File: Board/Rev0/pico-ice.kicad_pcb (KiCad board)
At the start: 2 copper layers, 52 x 51 mm, 121 parts, among them J1 Connector_USB_B_Micro, J1 USB_B_Micro, J2 6X2 Female Header, J2 Conn_01x02, J3 6X2 Female Header, J3 Conn_02x18_Odd_Even, J4 6X2 Female Header, J4 Conn_02x18_Odd_Even, J5 Conn_ARM_JTAG_SWD_10, J6 6X2 Female Header, J7 6X2 Female Header, J8 6X2 Female Header, J9 BOOT_SEL, SW1 PTS820 J25K SMTR LFS, SW2 PTS820 J25K SMTR LFS, U1 NCP1117ST33T3G, U2 W25Q128JVS, U2 W25Q32JVSSIQ, U3 RP2040, U4 CL9293A12L5M, U5 APS6404L-3SQN-SN, U6 ICE40UP5K-SG48ITR, U8 W25Q32JVSSIQ, Y1 ABLS-12.000MHZ-B4-T

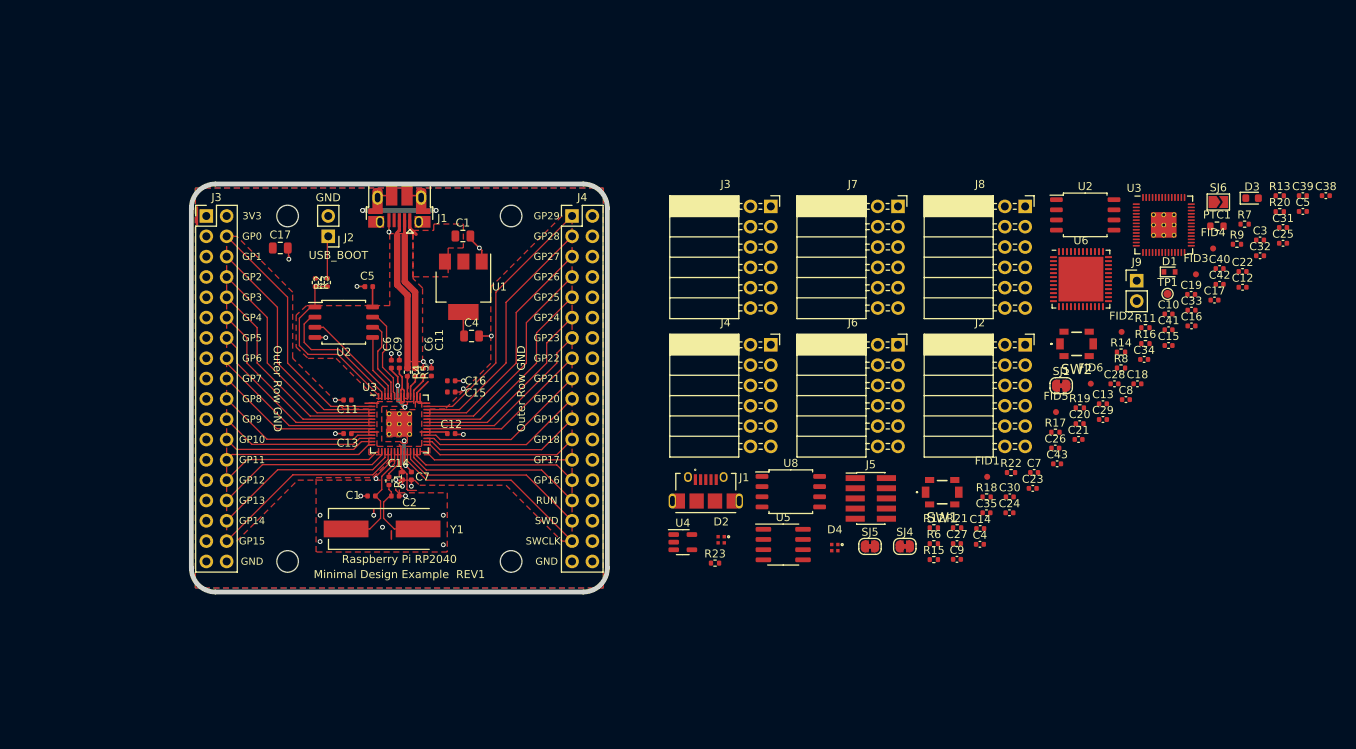
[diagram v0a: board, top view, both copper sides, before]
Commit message: Rough placement, needs work to compress this and center everything into 0.1" centers
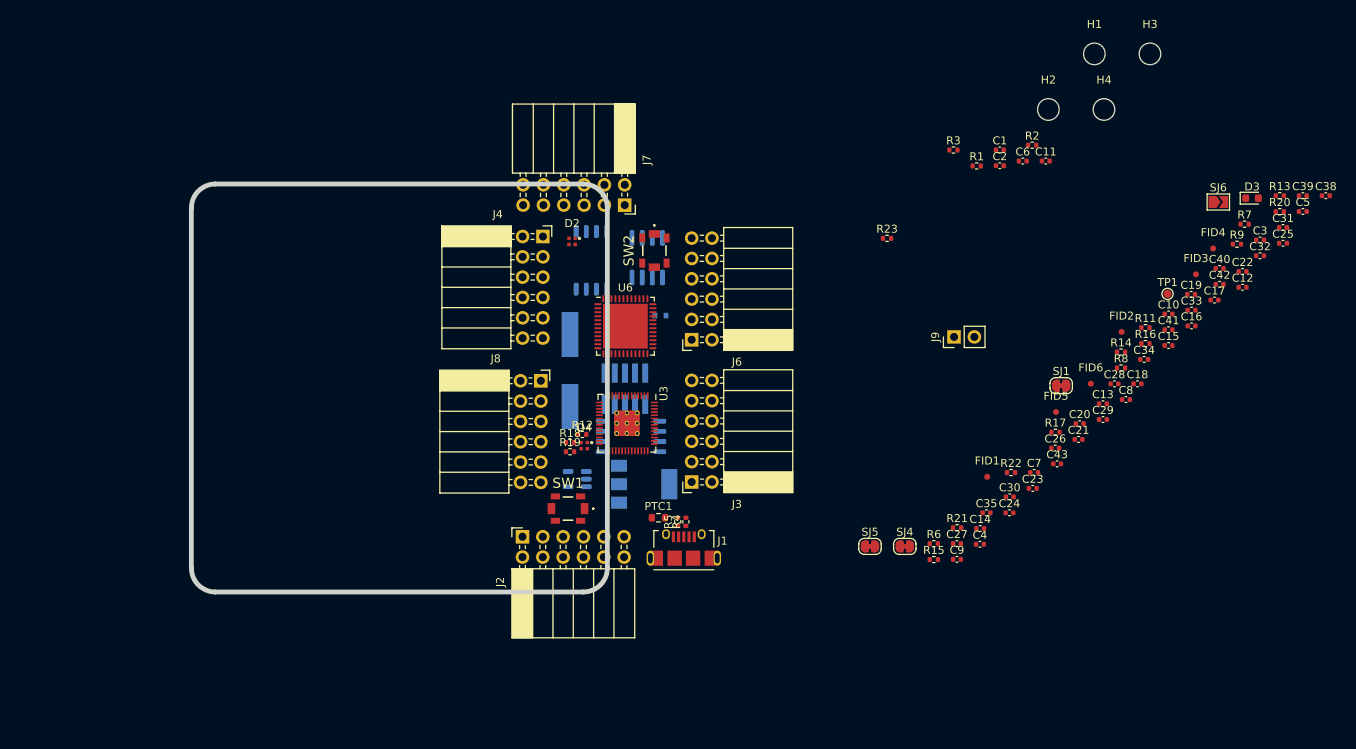
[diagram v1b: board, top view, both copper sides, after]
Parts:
- removed the C1 at (107.9, 76.5)
- removed the C1 at (96.5, 109.0)
- removed the C11 at (104.0, 93.5)
- removed the C11 at (93.5, 97.0)
- removed the C12 at (106.5, 101.2)
- removed the C13 at (93.5, 101.2)
- removed the C14 at (100.4, 106.5)
- removed the C15 at (106.5, 96.0)
- removed the C16 at (106.5, 94.6)
- removed the C17 at (85.1, 78.0)
- removed the C4 at (109.0, 89.0)
- removed the C5 at (96.2, 82.8)
- removed the C6 at (103.0, 93.5)
- removed the C6 at (99.0, 92.5)
- removed the C7 at (101.5, 106.5)
- removed the C9 at (100.0, 92.5)
- removed the J1 at (100.0, 71.7)
- removed the J2 at (91.1, 76.5)
- removed the J3 at (75.9, 74.0)
- removed the J4 at (121.6, 74.0)
- removed the U2 at (93.0, 87.3)
- removed the U3 at (100.0, 100.0)
- added C1: 27p, Capacitor_SMD:C_0402_1005Metric, F.Cu at (175.1, 65.7)
- added C11: 1u, Capacitor_SMD:C_0402_1005Metric, F.Cu at (180.8, 67.1)
- added C6: 1u, Capacitor_SMD:C_0402_1005Metric, F.Cu at (177.9, 67.1)
- D1, J5, U1, U2, U4, U5, U8, Y1: moved to B.Cu
- moved H4 116.6 mm to (188.1, 60.7)
- moved H1 102.9 mm to (186.9, 53.7)
- moved H3 102.0 mm to (193.8, 53.7)
- moved R2 89.8 mm to (179.1, 65.2), turned to 0 degrees
- moved C2 86.1 mm to (175.1, 67.7)
- moved R1 83.4 mm to (172.2, 67.7), turned to 0 degrees
- moved R3 81.5 mm to (169.3, 65.8), turned to 0 degrees
- moved PTC1 78.8 mm to (132.4, 111.7)
- moved U3 71.5 mm to (128.4, 99.9), turned to -90 degrees
- moved H2 68.5 mm to (181.1, 60.7)
- moved J2 67.3 mm to (115.4, 114.1), turned to 90 degrees
- moved J8 64.3 mm to (117.7, 94.6)
- moved R19 64.0 mm to (121.3, 103.5)
- moved D1 63.9 mm to (132.6, 86.4), turned to 180 degrees
- moved U2 63.2 mm to (129.0, 101.6)
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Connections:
- J2 pad a1: /ADC1 -> /~{RESET}
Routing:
- net +3V3: track 45.2 -> 0.00 mm, vias 2 -> 0
- net GND: track 34.8 -> 0.00 mm, vias 28 -> 0
- net /GPIO29_ADC3: track 33.2 -> 0.00 mm
- net /GPIO0: track 31.8 -> 0.00 mm
- net /GPIO28_ADC2: track 31.6 -> 0.00 mm
- net /GPIO1: track 30.2 -> 0.00 mm
- net /GPIO27_ADC1: track 29.9 -> 0.00 mm
- net /GPIO2: track 28.5 -> 0.00 mm
- net /GPIO26_ADC0: track 28.3 -> 0.00 mm
- net /GPIO3: track 26.9 -> 0.00 mm
- net /GPIO25: track 26.7 -> 0.00 mm
- net /SWCLK: track 25.9 -> 0.00 mm
- net /GPIO15: track 25.4 -> 0.00 mm
- net /GPIO4: track 25.3 -> 0.00 mm
- net /GPIO24: track 25.0 -> 0.00 mm
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- removed copper zone on F.Cu, net +1V1
- removed copper zone on F.Cu, net +3V3
- removed copper zone on B.Cu, net GND
- removed copper zone on F.Cu, net GND
- removed copper zone on F.Cu, net VBUS
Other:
- board text removed: "3V3"
- board text removed: "GND"
- board text removed: "GP0"
- board text removed: "GP1"
- board text removed: "GP10"
- board text removed: "GP11"
- board text removed: "GP12"
- board text removed: "GP13"
- board text removed: "GP14"
- board text removed: "GP15"
- board text removed: "GP16"
- board text removed: "GP17"
- board text removed: "GP18"
- board text removed: "GP19"
- board text removed: "GP2"
- board text removed: "GP20"
- board text removed: "GP21"
- board text removed: "GP22"
- board text removed: "GP23"
- board text removed: "GP24"
- board text removed: "GP25"
- board text removed: "GP26"
- board text removed: "GP27"
- board text removed: "GP28"
- board text removed: "GP29"
- board text removed: "GP3"
- board text removed: "GP4"
- board text removed: "GP5"
- board text removed: "GP6"
- board text removed: "GP7"
- board text removed: "GP8"
- board text removed: "GP9"
- board text removed: "Minimal Design Example REV1"
- board text removed: "Outer Row GND"
- board text removed: "RUN"
- board text removed: "Raspberry Pi RP2040"
- board text removed: "SWCLK"
- board text removed: "SWD"
- board text removed: "USB_BOOT"

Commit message: Finished the preliminary placement.
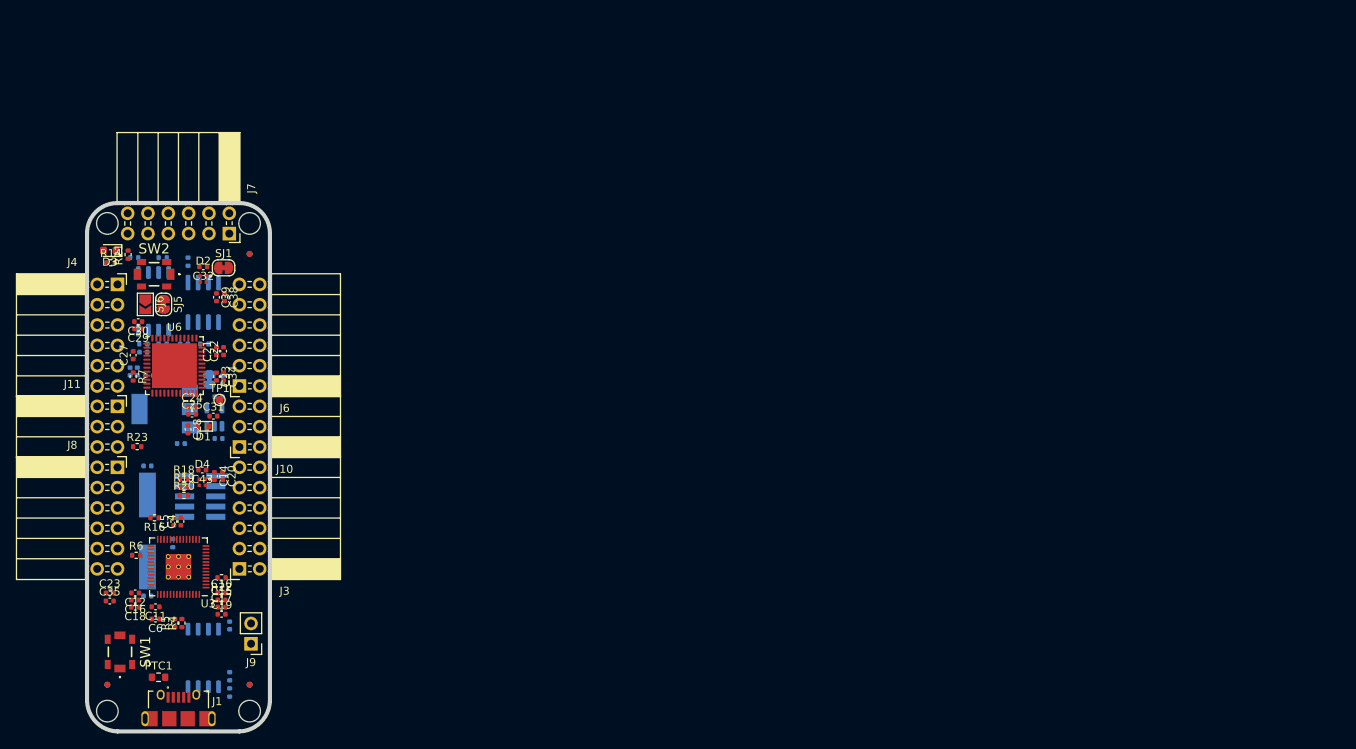
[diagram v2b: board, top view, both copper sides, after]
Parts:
- removed J2: 6X2 Female Header, CUSTOM:PMOD_2x06_P2.54mm_Horizontal
- added J10: 2x3_2.54mm_Female, Connector_PinSocket_2.54mm:PinSocket_2x03_P2.54mm_Horizontal, F.Cu at (80.0, 102.9)
- added J11: 2x3_2.54mm_Female, Connector_PinSocket_2.54mm:PinSocket_2x03_P2.54mm_Horizontal, F.Cu at (64.8, 97.8)
- C1, C13, C2, C26, C3, C40, C41, C42, C7, C8, C9, FID2, FID4, FID6, R1, R11, R12, R13, R15, R17, R2, R3, R8, R9, SJ4: moved to B.Cu
- D1: moved to F.Cu
- moved C5 146.4 mm to (71.8, 112.2), turned to 90 degrees
- moved H4 145.5 mm to (63.5, 135.9)
- moved C12 143.6 mm to (67.0, 121.1), turned to 180 degrees
- moved R13 143.3 mm to (68.0, 90.0), turned to 180 degrees
- moved D3 142.9 mm to (63.8, 78.3), turned to 180 degrees
- moved R20 141.5 mm to (73.1, 108.9)
- moved R7 140.2 mm to (66.7, 94.1), turned to -90 degrees
- moved H3 139.3 mm to (81.3, 135.9)
- moved C38 138.2 mm to (78.2, 84.2), turned to -90 degrees
- moved C25 138.0 mm to (74.1, 98.8)
- moved C3 137.3 mm to (72.7, 102.4), turned to 180 degrees
- moved C40 136.8 mm to (66.3, 93.4), turned to 90 degrees
- moved C16 136.4 mm to (67.0, 122.0), turned to 180 degrees
- moved C39 136.4 mm to (77.1, 84.2), turned to -90 degrees
- moved C31 135.8 mm to (76.8, 99.0)
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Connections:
- SW1 pad SH1: (no net) -> GND
- SW1 pad SH2: (no net) -> /~{RESET}
- SW2 pad SH1: (no net) -> +3V3
- SW2 pad SH2: (no net) -> /ICE_10|PB
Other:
- board size 52 x 51 mm -> 22.9 x 66 mm

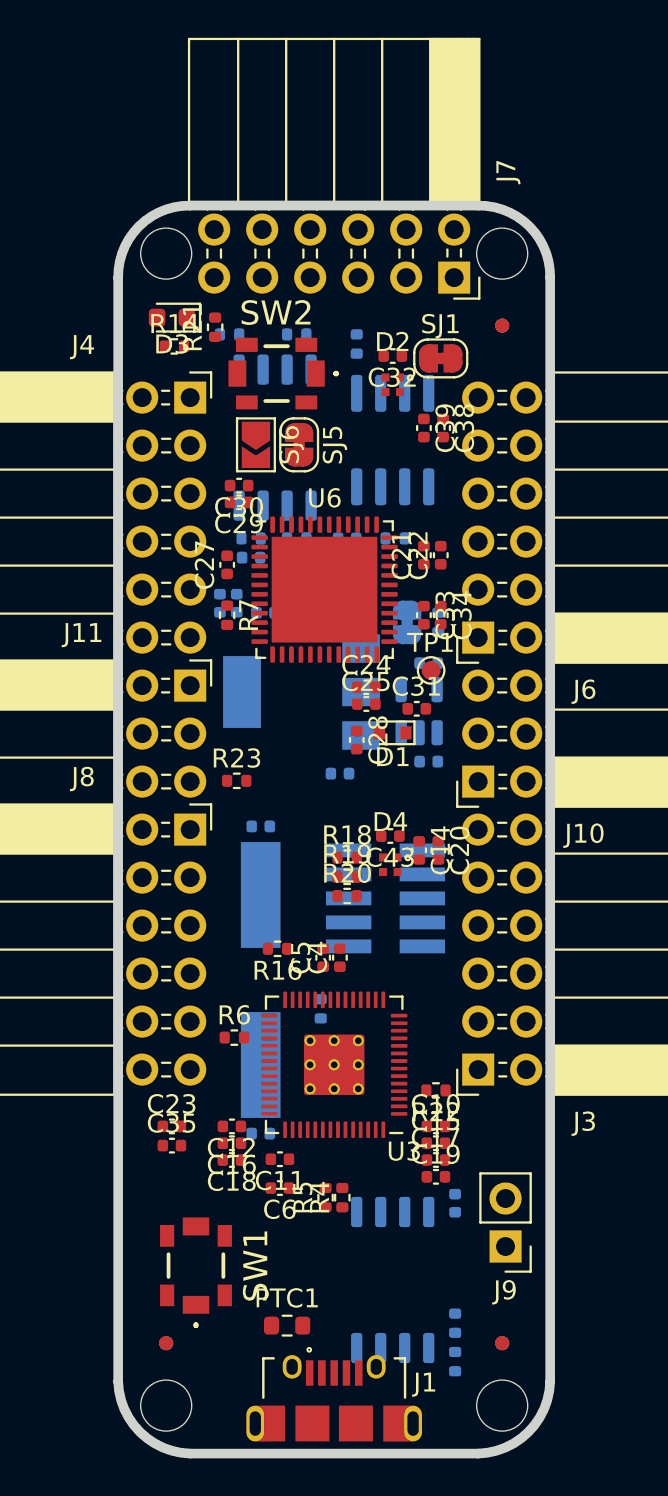
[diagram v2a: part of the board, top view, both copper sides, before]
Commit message: Reduce the board outline.
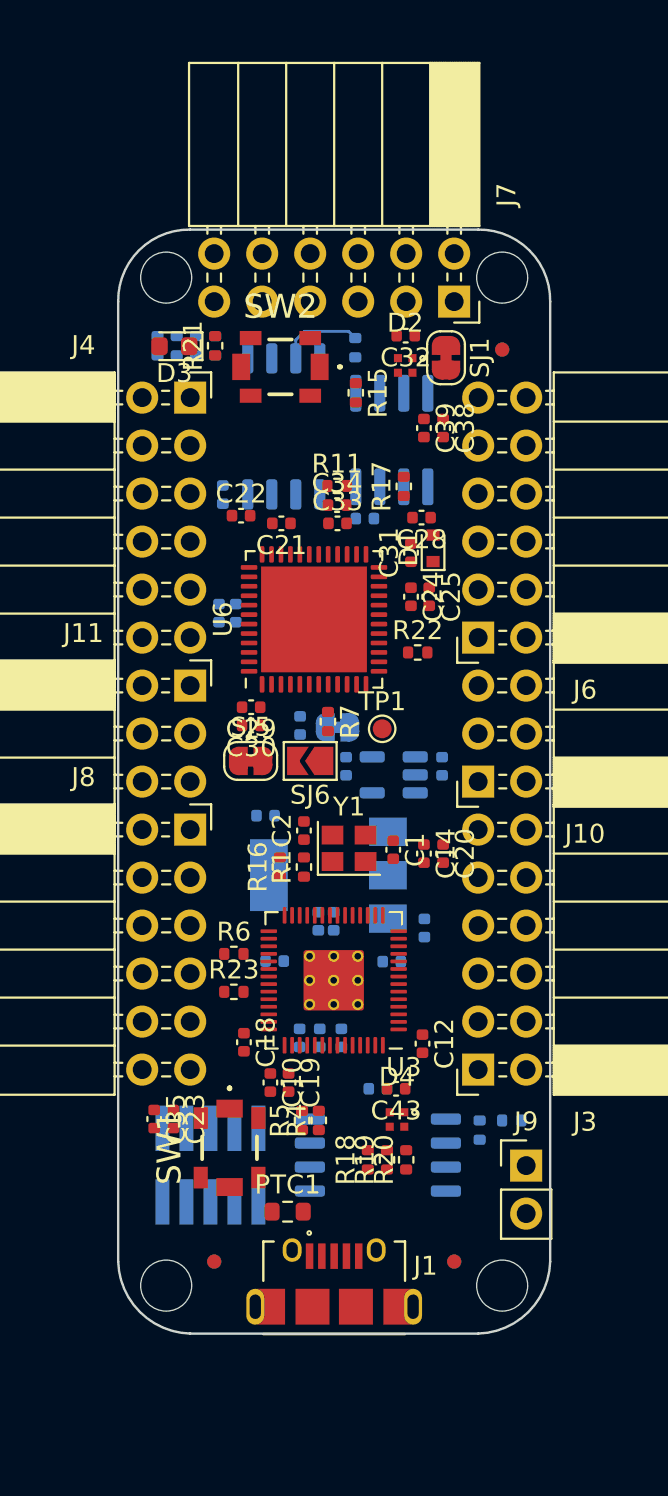
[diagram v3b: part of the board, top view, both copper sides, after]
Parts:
- C1, C2, R1, R11, R15, R17: moved to F.Cu
- C11, C15, C16, C17, C27, C4, C5, C6, R14: moved to B.Cu
- Y1: value ABLS-12.000MHZ-B4-T -> 12 MHz; footprint RP2040_minimal:Crystal_SMD_HC49-US -> Crystal:Crystal_SMD_2520-4Pin_2.5x2.0mm; moved to F.Cu
- moved R22 23.2 mm to (76.8, 96.0), turned to 0 degrees
- moved SJ6 17.0 mm to (71.1, 101.8), turned to 180 degrees
- moved SJ5 16.9 mm to (68.0, 101.8), turned to 0 degrees
- moved J5 16.9 mm to (65.8, 123.2), turned to -90 degrees
- moved C2 16.2 mm to (70.8, 105.5), turned to 90 degrees
- moved R18 16.0 mm to (74.2, 122.9), turned to 90 degrees
- moved R19 15.1 mm to (75.2, 122.9), turned to 90 degrees
- moved R20 14.3 mm to (76.2, 122.9), turned to 90 degrees
- moved C17 13.6 mm to (69.2, 112.4)
- moved D4 13.5 mm to (75.7, 120.8)
- moved C43 13.4 mm to (75.7, 119.1)
- moved R2 13.1 mm to (81.8, 120.8), turned to 0 degrees
- moved C16 12.9 mm to (72.4, 110.3), turned to -90 degrees
- moved C30 12.7 mm to (68.0, 99.9)
- moved C28 12.3 mm to (77.0, 88.9), turned to 180 degrees
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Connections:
- J10 pad 2: /ICE_35_G0 -> /~{RESET}
- J10 pad 3: /SRAM_SSN -> /PICO_CLKOUT
- J11 pad 5: /PICO_CLKOUT -> /SRAM_SSN
- J11 pad 6: /~{RESET} -> /ICE_35_G0
- SW1 pad SH1: GND -> unconnected-(SW1-PadSH1)
- SW1 pad SH2: /~{RESET} -> unconnected-(SW1-PadSH2)
- SW2 pad SH1: +3V3 -> unconnected-(SW2-PadSH1)
- SW2 pad SH2: /ICE_10|PB -> unconnected-(SW2-PadSH2)
- Y1 pad 1: /XIN -> Net-(C2-Pad1)
- Y1 pad 2: Net-(C2-Pad1) -> GND
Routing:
- net /ICE_FLASH_IO2: track 0.00 -> 4.46 mm
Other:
- board size 22.9 x 66 mm -> 22.9 x 58.4 mm

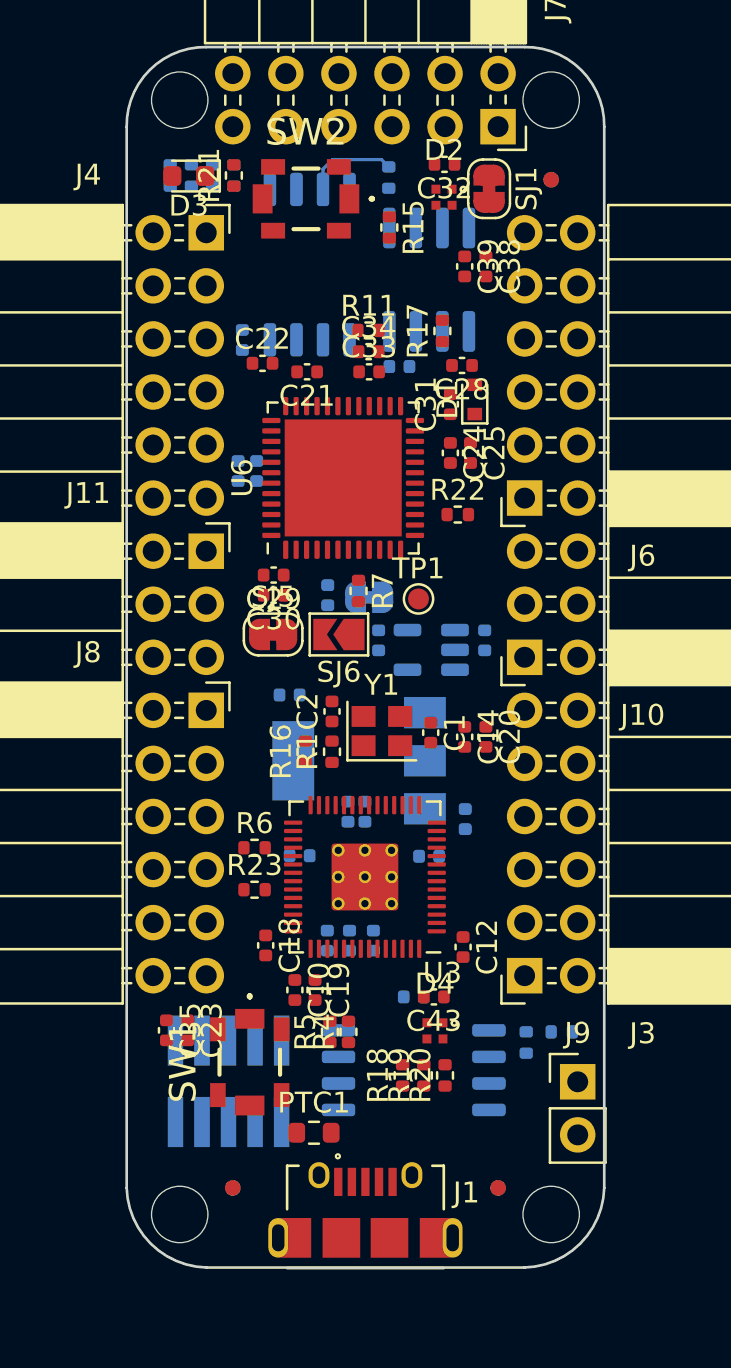
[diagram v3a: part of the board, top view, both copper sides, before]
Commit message: Replaced USB connector.
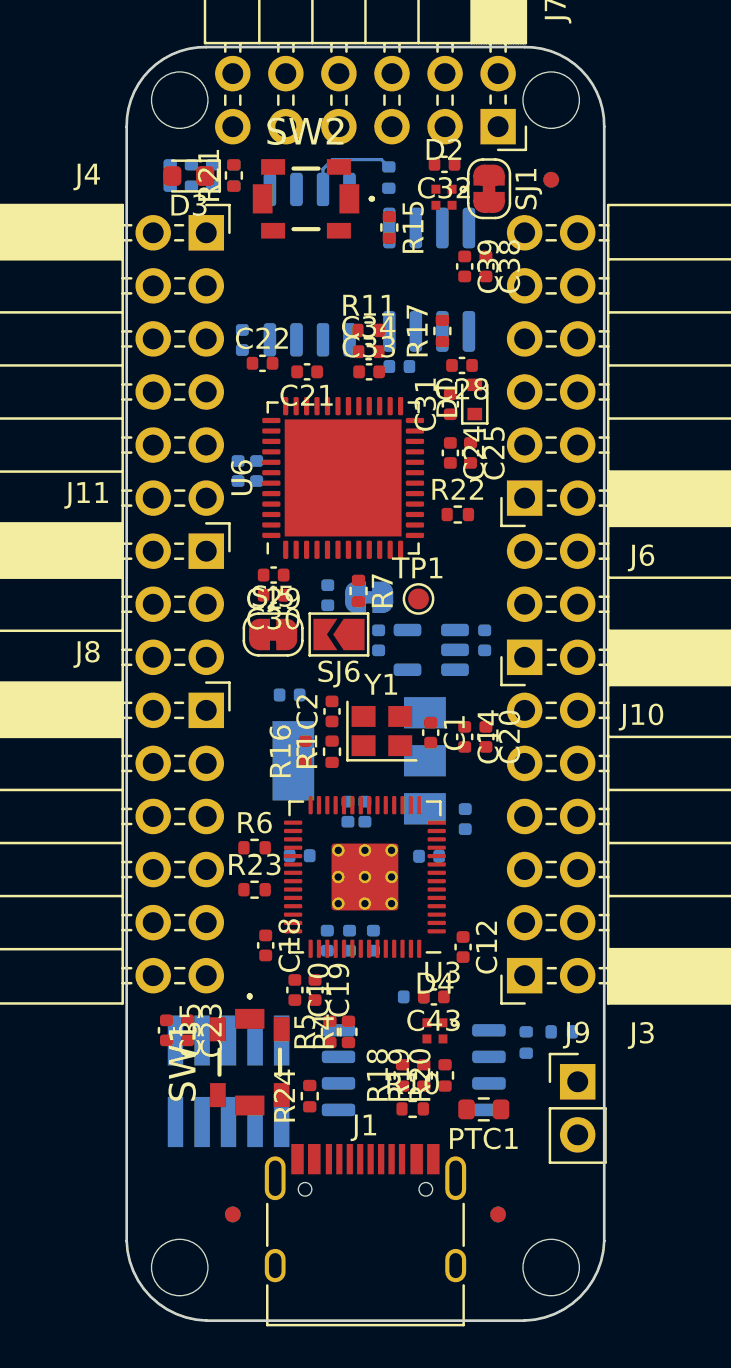
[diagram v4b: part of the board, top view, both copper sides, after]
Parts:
- added R10: 5.1K, Resistor_SMD:R_0402_1005Metric, F.Cu at (74.7, 124.5)
- added R24: 5.1K, Resistor_SMD:R_0402_1005Metric, F.Cu at (69.7, 123.9)
- J1: value Connector_USB_B_Micro -> USB_C_Receptacle_USB2.0; footprint CUSTOM:MOLEX_47589-0001 -> Connector_USB:USB_C_Receptacle_HRO_TYPE-C-31-M-12
- moved PTC1 8.20 mm to (78.1, 124.5), turned to 180 degrees
- moved H3 2.54 mm to (81.3, 132.1)
- moved H4 2.54 mm to (63.5, 132.1)
- moved FID3 1.27 mm to (78.7, 129.5)
- moved FID4 1.27 mm to (78.7, 129.5)
- moved FID5 1.27 mm to (66.0, 129.5)
- moved FID6 1.27 mm to (66.0, 129.5)
- moved J1 1.02 mm to (72.4, 130.9)
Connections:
- PTC1 pad 2: Net-(J1-Pad1) -> Net-(PTC1-Pad2)
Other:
- board size 22.9 x 58.4 mm -> 22.9 x 61 mm
